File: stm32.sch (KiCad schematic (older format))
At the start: 18 parts, among them CON1 BARREL_JACK, P1 CONN_01X11, P2 CONN_01X13, P3 CONN_01X08, P4 CONN_01X14, U1 STM32F103RB, U2 LD1117S33TR

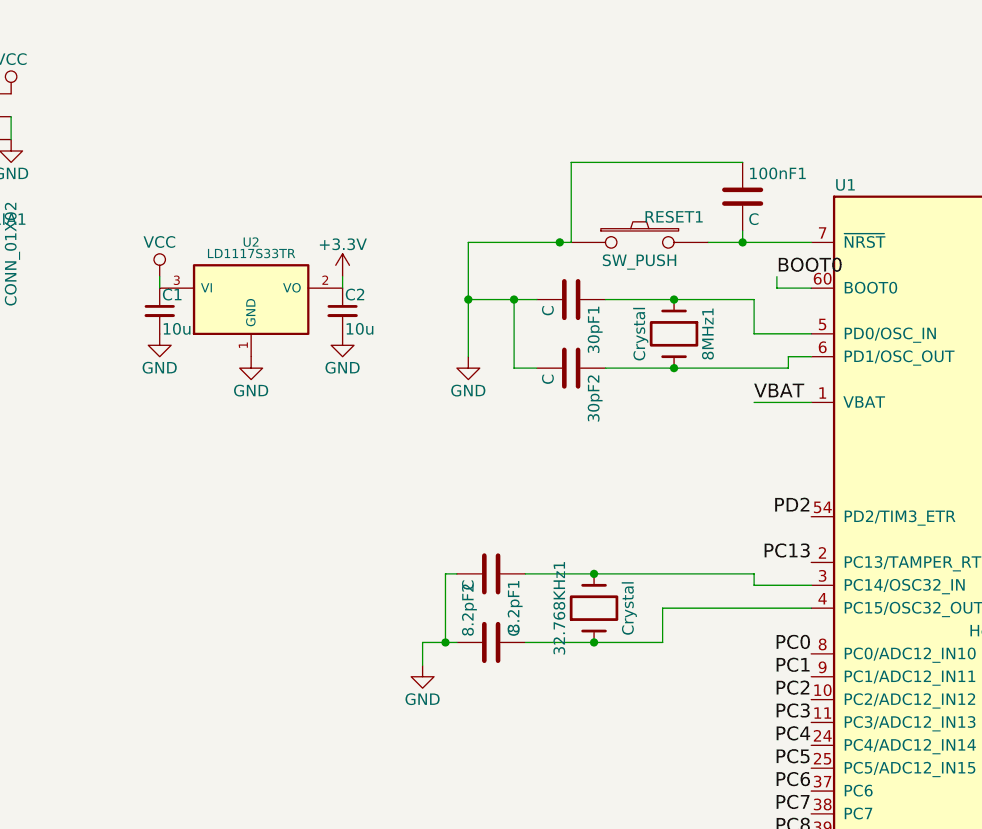
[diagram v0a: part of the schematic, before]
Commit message: ajustes
corrigido a inversão do valor com referencia
diminuido a largura da trilha.
trocado componentes por smd
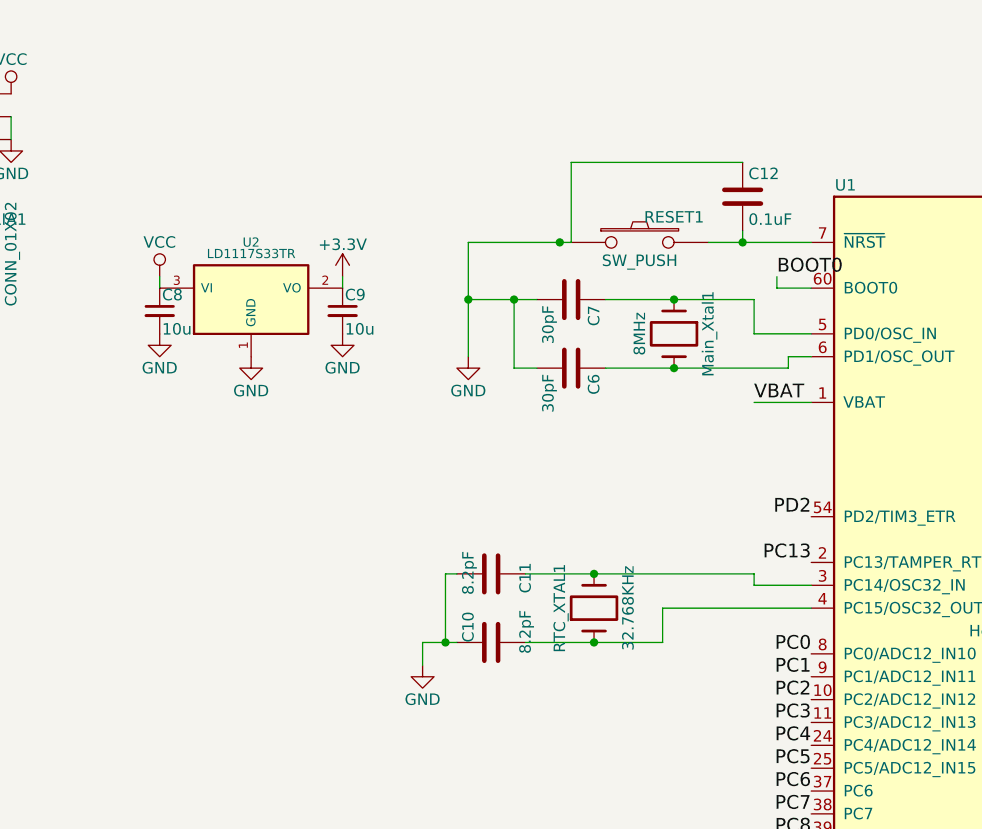
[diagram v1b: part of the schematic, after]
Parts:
- C10: renamed from 8.2pF2; value C -> 8.2pF
- C11: renamed from 8.2pF1; value C -> 8.2pF
- C12: renamed from 100nF1; value C -> 0.1uF
- C6: renamed from 30pF2; value C -> 30pF
- C7: renamed from 30pF1; value C -> 30pF
- Main_Xtal1: renamed from 8MHz1; value Crystal -> 8MHz
- RTC_XTAL1: renamed from 32.768KHz1; value Crystal -> 32.768KHz
- renumbered C1 to C8, C2 to C9
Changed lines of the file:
@@
 $EndComp
 $Comp
-L Crystal 32.768KHz1
+L Crystal RTC_XTAL1
 U 1 1 5717BE05
 P 3850 3950
-F 0 "32.768KHz1" H 3850 4100 50  0000 C CNN
-F 1 "Crystal" H 3850 3800 50  0000 C CNN
+F 0 "RTC_XTAL1" H 3850 4100 50  0000 C CNN
+F 1 "32.768KHz" H 3850 3800 50  0000 C CNN
 F 2 "Crystals:Crystal_Round_Vertical_3mm" H 3850 3950 50  0001 C CNN
 F 3 "" H 3850 3950 50  0000 C CNN
@@
 $EndComp
 $Comp
-L C 8.2pF1
+L C C11
 U 1 1 5717BF02
 P 3400 3800
-F 0 "8.2pF1" H 3425 3900 50  0000 L CNN
-F 1 "C" H 3425 3700 50  0000 L CNN
+F 0 "C11" H 3350 3950 50  0000 L CNN
+F 1 "8.2pF" H 3300 3700 50  0000 L CNN
 F 2 "Capacitors_SMD:C_0603_HandSoldering" H 3438 3650 50  0001 C CNN
 F 3 "" H 3400 3800 50  0000 C CNN
@@
 $EndComp
 $Comp
-L C 8.2pF2
+L C C10
 U 1 1 5717BFEF
 P 3400 4100
-F 0 "8.2pF2" H 3425 4200 50  0000 L CNN
-F 1 "C" H 3425 4000 50  0000 L CNN
+F 0 "C10" H 3400 4200 50  0000 L CNN
+F 1 "8.2pF" H 3350 3950 50  0000 L CNN
 F 2 "Capacitors_SMD:C_0603_HandSoldering" H 3438 3950 50  0001 C CNN
 F 3 "" H 3400 4100 50  0000 C CNN
@@
 $EndComp
 $Comp
-L GND #PWR01
+L GND #PWR12
 U 1 1 571807A9
 P 6000 6250
-F 0 "#PWR01" H 6000 6000 50  0001 C CNN
+F 0 "#PWR12" H 6000 6000 50  0001 C CNN
 F 1 "GND" H 6000 6100 50  0000 C CNN
 F 2 "" H 6000 6250 50  0000 C CNN
@@
 $EndComp
 $Comp
-L +3.3V #PWR02
+L +3.3V #PWR11
 U 1 1 57180F00
 P 5800 1950
-F 0 "#PWR02" H 5800 1800 50  0001 C CNN
+F 0 "#PWR11" H 5800 1800 50  0001 C CNN
 F 1 "+3.3V" H 5800 2090 50  0000 C CNN
 F 2 "" H 5800 1950 50  0000 C CNN
@@
 $EndComp
 $Comp
-L C 100nF1
+L C C12
 U 1 1 57182019
 P 4500 2150
-F 0 "100nF1" H 4525 2250 50  0000 L CNN
-F 1 "C" H 4525 2050 50  0000 L CNN
+F 0 "C12" H 4525 2250 50  0000 L CNN
+F 1 "0.1uF" H 4525 2050 50  0000 L CNN
 F 2 "Capacitors_SMD:C_0603_HandSoldering" H 4538 2000 50  0001 C CNN
 F 3 "" H 4500 2150 50  0000 C CNN
@@
 $EndComp
 $Comp
-L GND #PWR03
+L GND #PWR10
 U 1 1 571820A4
 P 3300 2850
-F 0 "#PWR03" H 3300 2600 50  0001 C CNN
+F 0 "#PWR10" H 3300 2600 50  0001 C CNN
 F 1 "GND" H 3300 2700 50  0000 C CNN
 F 2 "" H 3300 2850 50  0000 C CNN
@@
 $EndComp
 $Comp
-L GND #PWR04
+L GND #PWR9
 U 1 1 571823B8
 P 3100 4200
-F 0 "#PWR04" H 3100 3950 50  0001 C CNN
+F 0 "#PWR9" H 3100 3950 50  0001 C CNN
 F 1 "GND" H 3100 4050 50  0000 C CNN
 F 2 "" H 3100 4200 50  0000 C CNN
@@
 $EndComp
 $Comp
-L Crystal 8MHz1
+L Crystal Main_Xtal1
 U 1 1 57184B59
 P 4200 2750
-F 0 "8MHz1" H 4200 2900 50  0000 C CNN
-F 1 "Crystal" H 4200 2600 50  0000 C CNN
+F 0 "Main_Xtal1" H 4200 2900 50  0000 C CNN
+F 1 "8MHz" H 4200 2600 50  0000 C CNN
 F 2 "Crystals:HC-18UV" H 4200 2750 50  0001 C CNN
 F 3 "" H 4200 2750 50  0000 C CNN
@@
 $EndComp
 $Comp
-L C 30pF1
+L C C7
 U 1 1 57184FBE
 P 3750 2600
-F 0 "30pF1" H 3775 2700 50  0000 L CNN
-F 1 "C" H 3775 2500 50  0000 L CNN
+F 0 "C7" H 3775 2700 50  0000 L CNN
+F 1 "30pF" H 3775 2500 50  0000 L CNN
 F 2 "Capacitors_SMD:C_0603_HandSoldering" H 3788 2450 50  0001 C CNN
 F 3 "" H 3750 2600 50  0000 C CNN
@@
 $EndComp
 $Comp
-L C 30pF2
+L C C6
 U 1 1 571850E4
 P 3750 2900
-F 0 "30pF2" H 3775 3000 50  0000 L CNN
-F 1 "C" H 3775 2800 50  0000 L CNN
+F 0 "C6" H 3775 3000 50  0000 L CNN
+F 1 "30pF" H 3775 2800 50  0000 L CNN
 F 2 "Capacitors_SMD:C_0603_HandSoldering" H 3788 2750 50  0001 C CNN
 F 3 "" H 3750 2900 50  0000 C CNN
@@
 BOOT1
 $Comp
-L C_Small C1
+L C_Small C8
 U 1 1 5718F033
 P 1950 2650
-F 0 "C1" H 1960 2720 50  0000 L CNN
+F 0 "C8" H 1960 2720 50  0000 L CNN
 F 1 "10u" H 1960 2570 50  0000 L CNN
 F 2 "Capacitors_SMD:C_0603_HandSoldering" H 1950 2650 60  0001 C CNN
@@
 $EndComp
 $Comp
-L C_Small C2
+L C_Small C9
 U 1 1 5718F036
 P 2750 2650
-F 0 "C2" H 2760 2720 50  0000 L CNN
+F 0 "C9" H 2760 2720 50  0000 L CNN
 F 1 "10u" H 2760 2570 50  0000 L CNN
 F 2 "Capacitors_SMD:C_0603_HandSoldering" H 2750 2650 60  0001 C CNN
@@
 $EndComp
 $Comp
-L GND #PWR05
+L GND #PWR5
 U 1 1 5718F037
 P 1950 2750
-F 0 "#PWR05" H 1950 2500 50  0001 C CNN
+F 0 "#PWR5" H 1950 2500 50  0001 C CNN
 F 1 "GND" H 1950 2600 50  0000 C CNN
 F 2 "" H 1950 2750 60  0000 C CNN
@@
 $EndComp
 $Comp
-L GND #PWR06
+L GND #PWR8
 U 1 1 5718F038
 P 2750 2750
-F 0 "#PWR06" H 2750 2500 50  0001 C CNN
+F 0 "#PWR8" H 2750 2500 50  0001 C CNN
 F 1 "GND" H 2750 2600 50  0000 C CNN
 F 2 "" H 2750 2750 60  0000 C CNN
@@
 $EndComp
 $Comp
-L VCC #PWR07
+L VCC #PWR4
 U 1 1 5718F03A
 P 1950 2500
-F 0 "#PWR07" H 1950 2350 50  0001 C CNN
+F 0 "#PWR4" H 1950 2350 50  0001 C CNN
 F 1 "VCC" H 1950 2650 50  0000 C CNN
 F 2 "" H 1950 2500 60  0000 C CNN
@@
 $EndComp
 $Comp
-L GND #PWR08
+L GND #PWR6
 U 1 1 5718FECA
 P 2350 2850
-F 0 "#PWR08" H 2350 2600 50  0001 C CNN
+F 0 "#PWR6" H 2350 2600 50  0001 C CNN
 F 1 "GND" H 2350 2700 50  0000 C CNN
 F 2 "" H 2350 2850 50  0000 C CNN
@@
 $EndComp
 $Comp
-L +3.3V #PWR09
+L +3.3V #PWR7
 U 1 1 57191625
 P 2750 2500
-F 0 "#PWR09" H 2750 2350 50  0001 C CNN
+F 0 "#PWR7" H 2750 2350 50  0001 C CNN
 F 1 "+3.3V" H 2750 2640 50  0000 C CNN
 F 2 "" H 2750 2500 50  0000 C CNN
@@
 $EndComp
 $Comp
-L VCC #PWR010
+L VCC #PWR2
 U 1 1 571965FD
 P 1300 1700
-F 0 "#PWR010" H 1300 1550 50  0001 C CNN
+F 0 "#PWR2" H 1300 1550 50  0001 C CNN
 F 1 "VCC" H 1300 1850 50  0000 C CNN
 F 2 "" H 1300 1700 50  0000 C CNN
@@
 $EndComp
 $Comp
-L GND #PWR011
+L GND #PWR3
 U 1 1 5719663F
 P 1300 1900
-F 0 "#PWR011" H 1300 1650 50  0001 C CNN
+F 0 "#PWR3" H 1300 1650 50  0001 C CNN
 F 1 "GND" H 1300 1750 50  0000 C CNN
 F 2 "" H 1300 1900 50  0000 C CNN
@@
 $EndComp
 $Comp
-L GND #PWR012
+L GND #PWR1
 U 1 1 57198DA2
 P 1000 2450
-F 0 "#PWR012" H 1000 2200 50  0001 C CNN
+F 0 "#PWR1" H 1000 2200 50  0001 C CNN
 F 1 "GND" H 1000 2300 50  0000 C CNN
 F 2 "" H 1000 2450 50  0000 C CNN
